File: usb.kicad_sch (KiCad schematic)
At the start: 99 parts, among them U16 TPS2066TDGNRQ1, U17 USB7016_KDX, U18 TPS2066TDGNRQ1, U19 TPD4E05U06QDQARQ1_PASS, U20 WE-TVS-82400152, U21 WE-TVS-82400152, U22 TPD4E05U06QDQARQ1_PASS, U23 USB3310C-CP, U24 GSB3112311HR, U25 TPD4E05U06QDQARQ1_PASS, U26 WE-TVS-82400152, U27 WE-TVS-82400152, U28 TPD4E05U06QDQARQ1_PASS, U29 GSB3112311HR, Y4 ECS-2016MV-250-CN-TR3, Y5 ECS-2016MV-240-BN-TR3

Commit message: Added cosmetic changes to schematics (e.g. position of labels, designators)
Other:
- moved on the sheet: C39, C65, C70, C72, C81, C82, C86, Y4, Y5

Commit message: Bump date and revision
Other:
- title: USB PHY and HUB -> Kria K26 Devboard
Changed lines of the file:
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@@
   (paper "A3")
   (title_block
-    (title "USB PHY and HUB")
-    (date "2022-07-25")
-    (rev "1.1.0")
+    (title "Kria K26 Devboard")
+    (date "2023-02-15")
+    (rev "1.1.1")
     (comment 1 "www.antmicro.com")
     (comment 2 "Antmicro Ltd.")

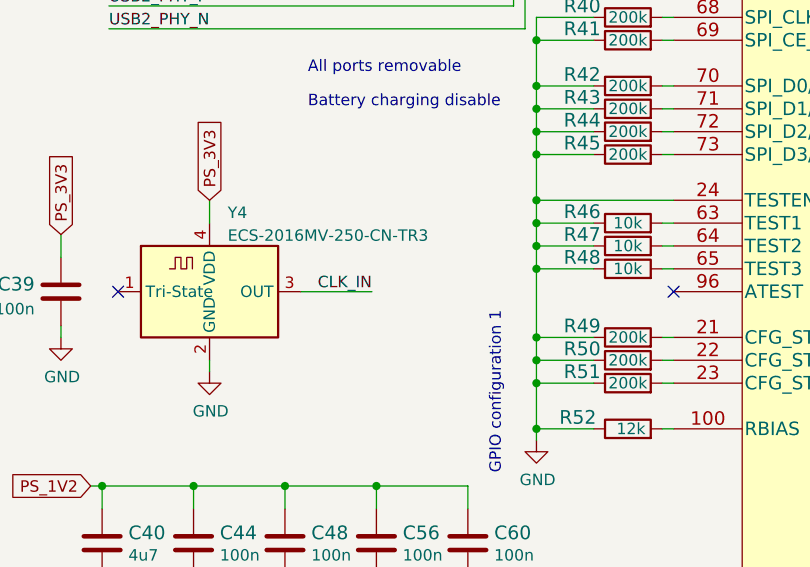
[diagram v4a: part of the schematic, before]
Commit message: Add missing USB7016 TEST1 pin pull-up
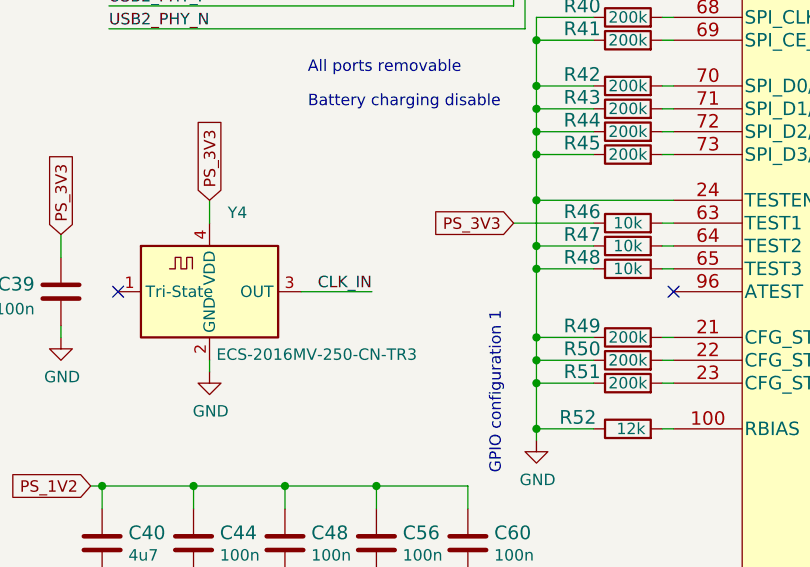
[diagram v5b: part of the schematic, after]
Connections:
- net GND: no longer R46.1
- net PS_3V3: now also R46.1
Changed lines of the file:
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@@
   (junction (at 35.56 149.86) (diameter 0) (color 0 0 0 0)
   )
-  (junction (at 73.66 99.06) (diameter 0) (color 0 0 0 0)
-  )
   (junction (at 304.8 85.09) (diameter 0) (color 0 0 0 0)
   )
@@
     (stroke (width 0) (type default) (color 0 0 0 0))
   )
-  (wire (pts (xy 73.66 101.6) (xy 73.66 99.06))
+  (wire (pts (xy 73.66 96.52) (xy 73.66 101.6))
     (stroke (width 0) (type default) (color 0 0 0 0))
   )
@@
     (stroke (width 0) (type default) (color 0 0 0 0))
   )
-  (wire (pts (xy 80.01 99.06) (xy 73.66 99.06))
-    (stroke (width 0) (type default) (color 0 0 0 0))
-  )
   (bus (pts (xy 264.16 48.26) (xy 264.16 52.07))
     (stroke (width 0) (type default) (color 0 0 0 0))
@@
     (stroke (width 0) (type default) (color 0 0 0 0))
   )
-  (wire (pts (xy 73.66 99.06) (xy 73.66 96.52))
-    (stroke (width 0) (type default) (color 0 0 0 0))
-  )
   (wire (pts (xy 261.62 25.4) (xy 267.97 25.4))
     (stroke (width 0) (type default) (color 0 0 0 0))
@@
     (stroke (width 0) (type default) (color 0 0 0 0))
   )
+  (wire (pts (xy 71.12 99.06) (xy 80.01 99.06))
+    (stroke (width 0) (type default) (color 0 0 0 0))
+  )
   (wire (pts (xy 35.56 138.43) (xy 35.56 140.97))
     (stroke (width 0) (type default) (color 0 0 0 0))
@@
     )
   )
+  (global_label "PS_3V3" (shape input) (at 71.12 99.06 180) (fields_autoplaced)
+    (effects (font (size 1.27 1.27)) (justify right))
+    (property "Intersheet References" "${INTERSHEET_REFS}" (id 0) (at 48.26 237.49 0)
+      (effects (font (size 1.27 1.27)) hide)
+    )
+  )
   (global_label "PS_3V3" (shape input) (at 24.13 175.26 180) (fields_autoplaced)
     (effects (font (size 1.27 1.27)) (justify right))
@@
   )
   (symbol (lib_id "kria-k26-devboard:ECS-2016MV-250-CN-TR3") (at 37.338 106.68 0) (unit 1)
-    (in_bom yes) (on_board yes) (fields_autoplaced)
+    (in_bom yes) (on_board yes)
     (property "Reference" "Y4" (id 0) (at 39.3574 97.9002 0)
       (effects (font (size 1.27 1.27)) (justify left))
     )
-    (property "Value" "ECS-2016MV-250-CN-TR3" (id 1) (at 39.3574 100.4371 0)
+    (property "Value" "ECS-2016MV-250-CN-TR3" (id 1) (at 38.1 113.665 0)
       (effects (font (size 1.27 1.27)) (justify left))
     )

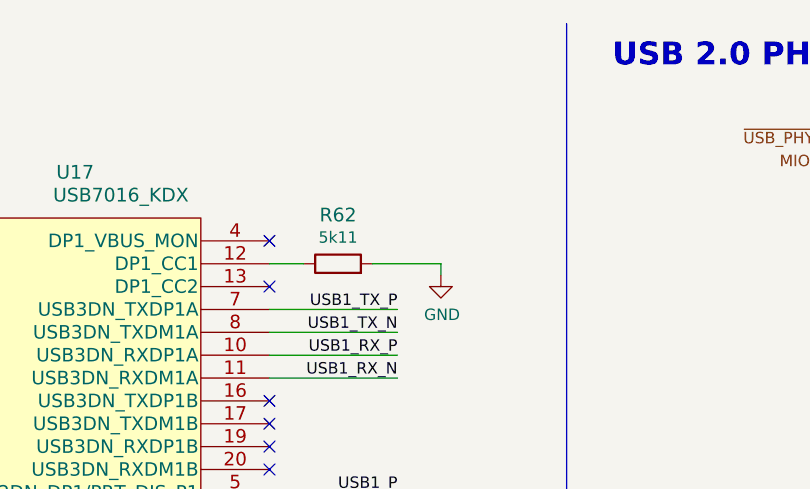
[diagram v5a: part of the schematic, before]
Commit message: Replace FTDI 3V3 Regulator
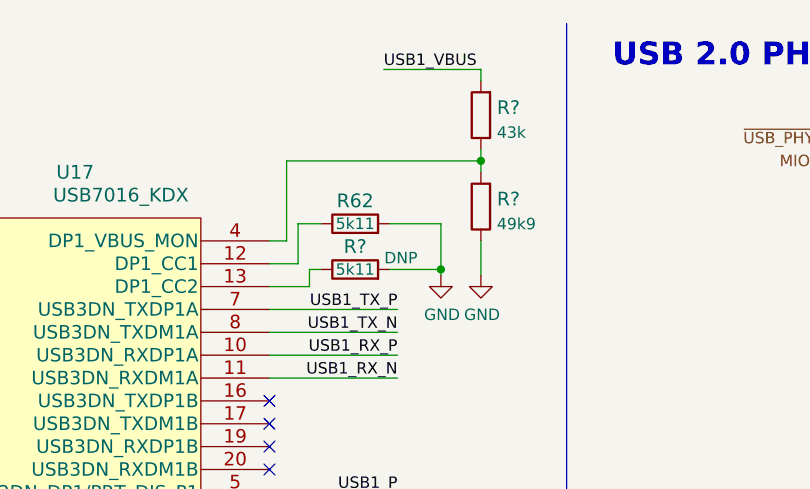
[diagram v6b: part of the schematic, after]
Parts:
- added R?: R_43k_0402, antmicro-footprints:0402-res, symbol antmicroResistors0402:R_43k_0402
- added R?: R_5k11_0402, kria-k26-devboard-footprints:0402-res, symbol kria-k26-devboard:R_5k11_0402
- added R?: R_49k9_0402, antmicro-footprints:0402-res, symbol antmicroResistors0402:R_49k9_0402
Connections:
- net GND: now also R?.1, R?.2
- net USB1_VBUS: now also R?.2
- net at U17.13 (DP1_CC2): now also R?.1
- net at U17.4 (DP1_VBUS_MON): now also R?.1, R?.2
- no-connect marks 18 -> 16
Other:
- moved on the sheet: R62

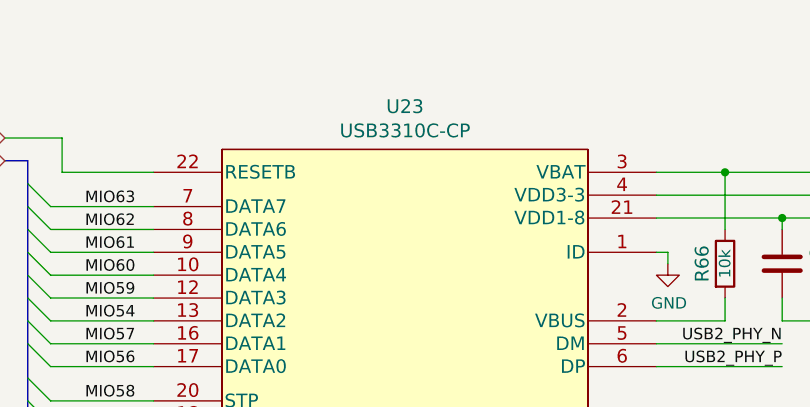
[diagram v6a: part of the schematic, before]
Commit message: Fix USB3310C symbol
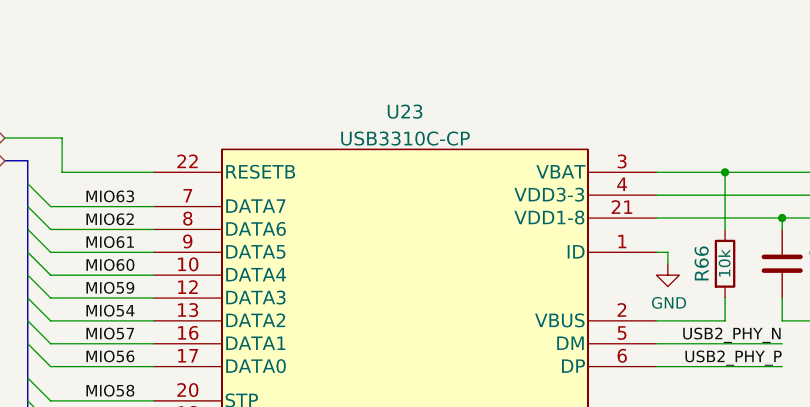
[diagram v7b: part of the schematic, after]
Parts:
- removed U23: USB3310C-CP, kria-k26-devboard-footprints:Microchip_QFN24_4X4, symbol kria-k26-devboard:USB3310C-CP
- added U23: USB3310C-CP, antmicro-footprints:Microchip_QFN24_4X4, symbol antmicroInterfaceControllers:USB3310C-CP
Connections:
- net GND: now also U23.1 (ID), U23.25 (EPAD)
- net MIO52: now also U23.11 (CLKOUT)
- net MIO53: now also U23.19 (DIR)
- net MIO54: now also U23.13 (DATA2)
- net MIO55: now also U23.18 (NXT)
- net MIO56: now also U23.17 (DATA0)
- net MIO57: now also U23.16 (DATA1)
- net MIO58: now also U23.20 (STP)
- net MIO59: now also U23.12 (DATA3)
- net MIO60: now also U23.10 (DATA4)
- net MIO61: now also U23.9 (DATA5)
- net MIO62: now also U23.8 (DATA6)
- net MIO63: now also U23.7 (DATA7)
- net PS_1V8: now also U23.14 (REFSEL1), U23.15 (REFSEL0), U23.21 (VDD1-8)
- net SOM_5V0: now also U23.3 (VBAT)
- net USB2_PHY_N: now also U23.5 (DM)
- net USB2_PHY_P: now also U23.6 (DP)
- net USB2_REFCLK: now also U23.23 (REFCLK)
- net ~{USB_PHY_RESET}: now also U23.22 (RESETB)
- net at R66.2: now also U23.2 (VBUS)
- net at R65.1: now also U23.24 (RBIAS)
- net at C86.1: now also U23.4 (VDD3-3)

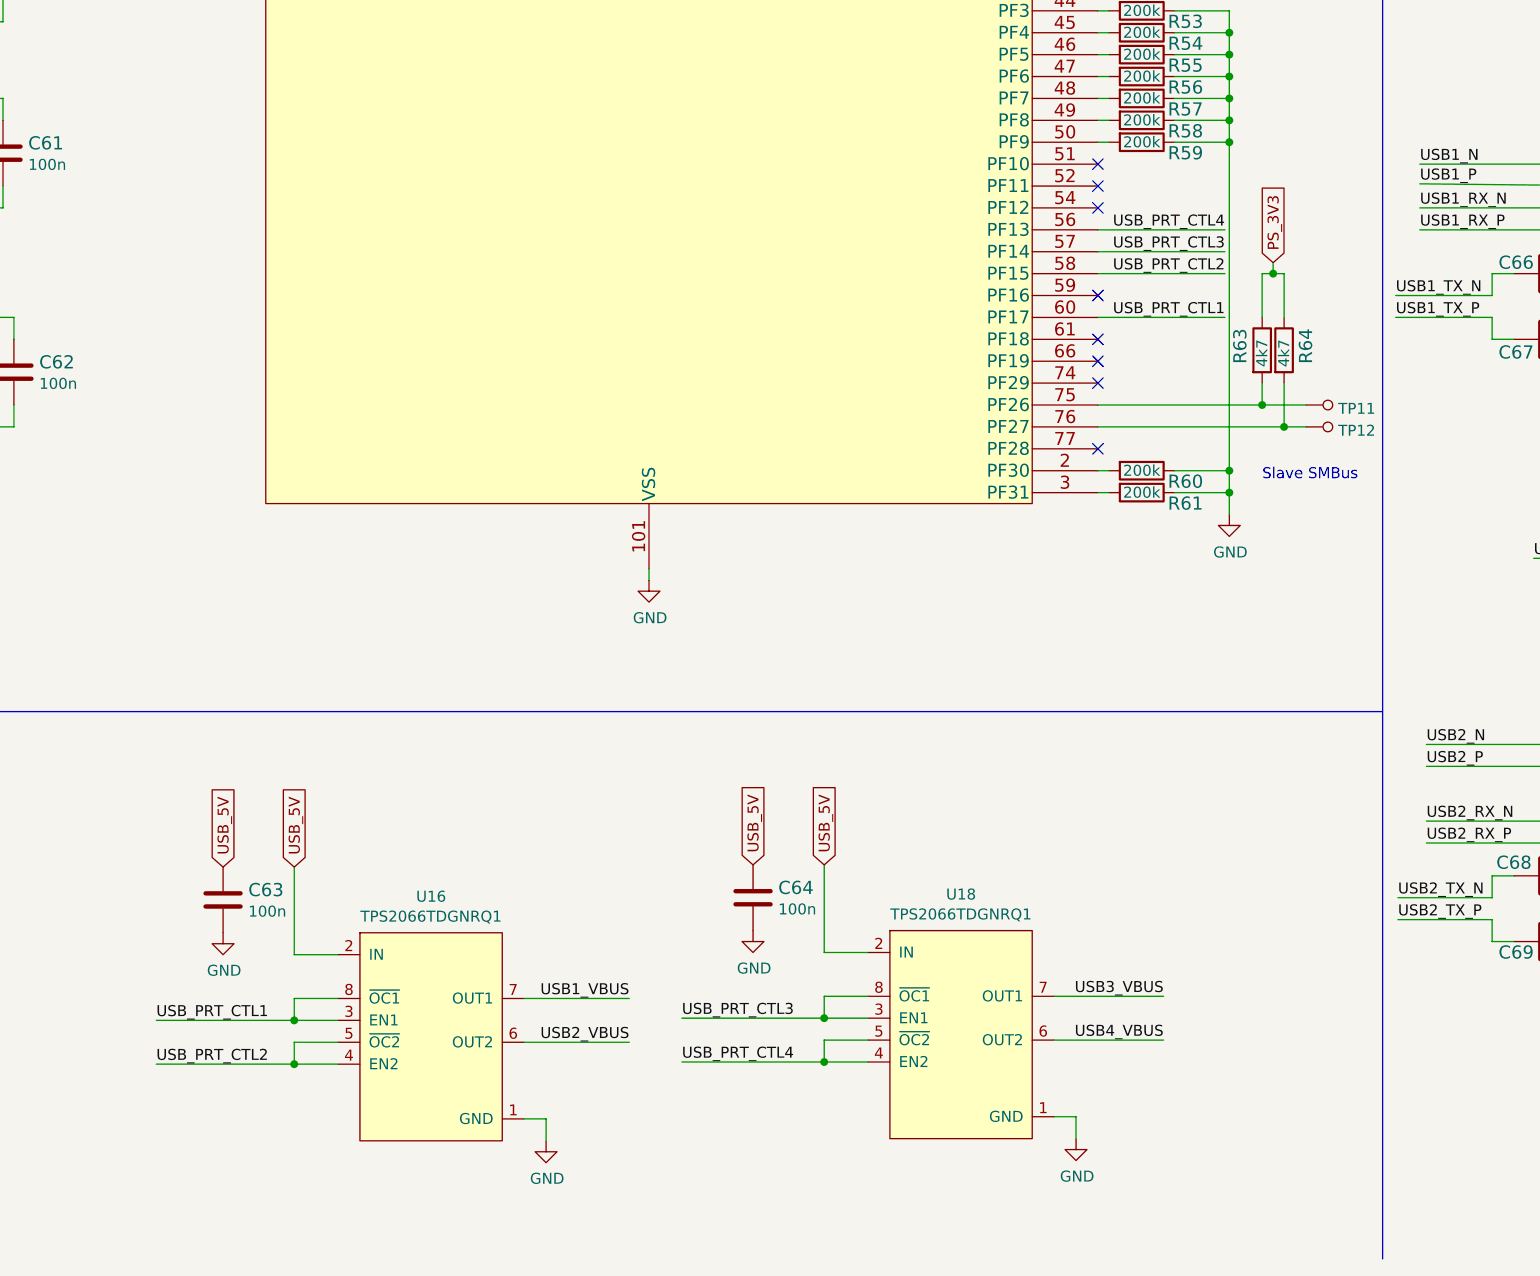
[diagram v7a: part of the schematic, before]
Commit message: Fix TPS2066 symbol
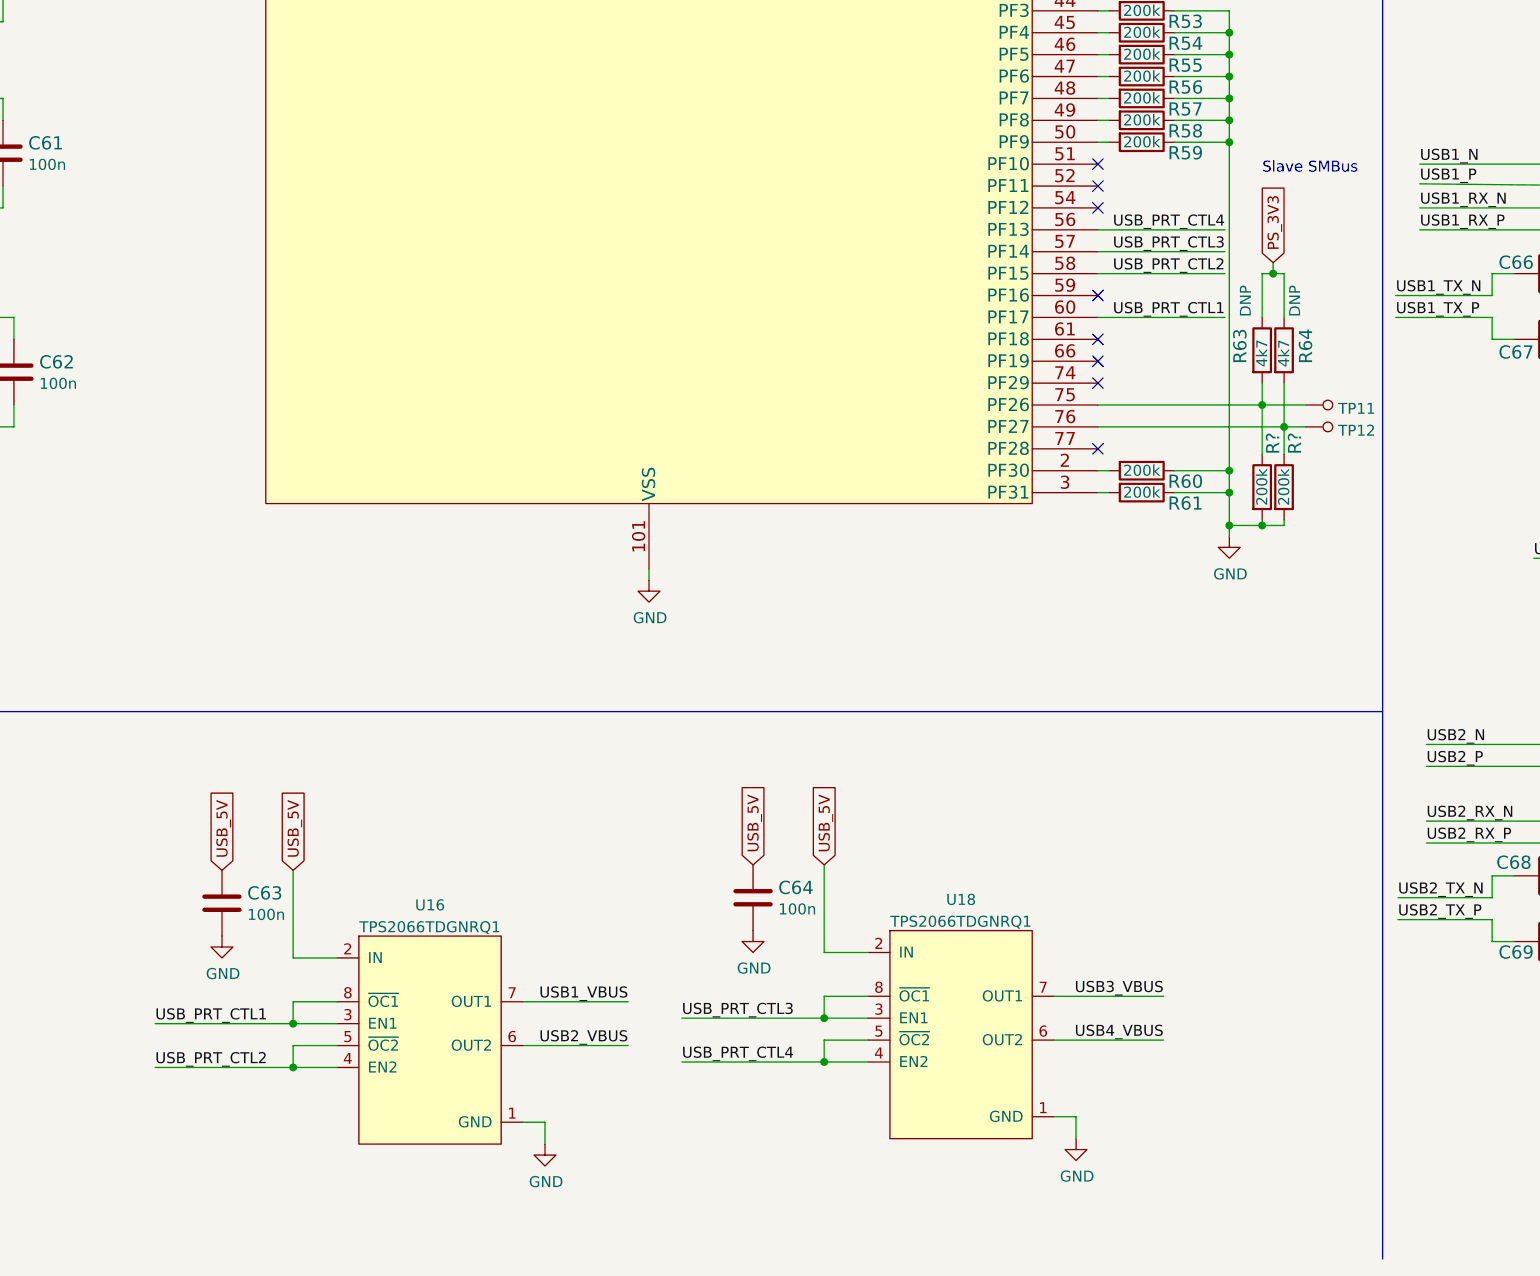
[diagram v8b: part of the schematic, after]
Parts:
- removed U16, U18: TPS2066TDGNRQ1, kria-k26-devboard-footprints:SOP65P490X110-9N, symbol kria-k26-devboard:TPS2066TDGNRQ1
- added R? (x2): R_200k_0402, kria-k26-devboard-footprints:0402-res, symbol kria-k26-devboard:R_200k_0402
- added U16, U18: TPS2066TDGNRQ1, antmicro-footprints:SOP65P490X110-9N, symbol antmicroPMICPowerDistributionSwitchesLoadDrivers:TPS2066TDGNRQ1
- R63, R64: DNP (none) -> DNP
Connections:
- net GND: now also R?.2, R?.2, U16.1 (GND), U18.1 (GND)
- net USB1_VBUS: now also U16.7 (OUT1)
- net USB2_VBUS: now also U16.6 (OUT2)
- net USB3_VBUS: now also U18.7 (OUT1)
- net USB4_VBUS: now also U18.6 (OUT2)
- net USB_5V: now also U16.2 (IN), U18.2 (IN)
- net USB_PRT_CTL1: now also U16.3 (EN1), U16.8 (~{OC1})
- net USB_PRT_CTL2: now also U16.4 (EN2), U16.5 (~{OC2})
- net USB_PRT_CTL3: now also U18.3 (EN1), U18.8 (~{OC1})
- net USB_PRT_CTL4: now also U18.4 (EN2), U18.5 (~{OC2})
- net at R63.2, TP11.1, U17.75 (PF26): now also R?.1
- net at R64.2, TP12.1, U17.76 (PF27): now also R?.1
